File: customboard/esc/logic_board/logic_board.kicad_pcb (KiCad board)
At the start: 4 copper layers, 18.3 x 28.1 mm, 112 parts, among them J1 Conn_01x11, J2 Conn_01x03, J3 Conn_01x06, J4 Conn_01x11, J5 Conn_01x02, J6 Conn_01x02, J7 Conn_01x06, J8 Conn_01x03, U1 STM32F051K8Ux, U2 DRV8300DRGE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

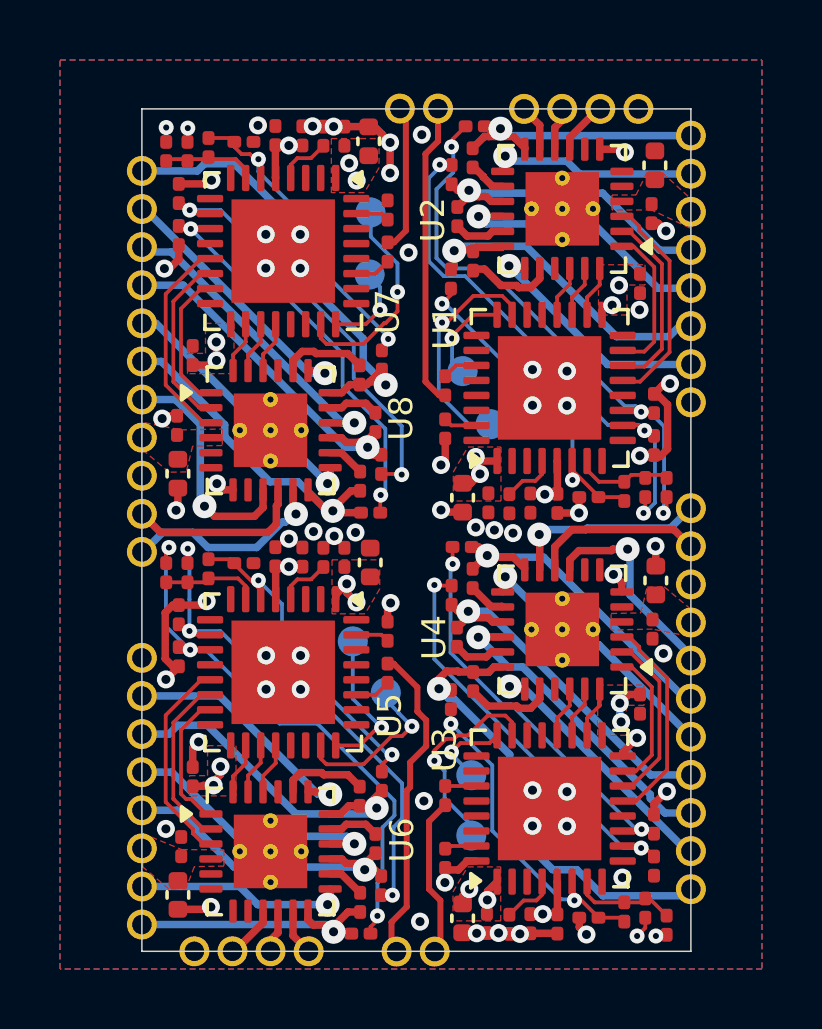
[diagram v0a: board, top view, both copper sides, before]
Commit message: power board done, minor fixes in logic board
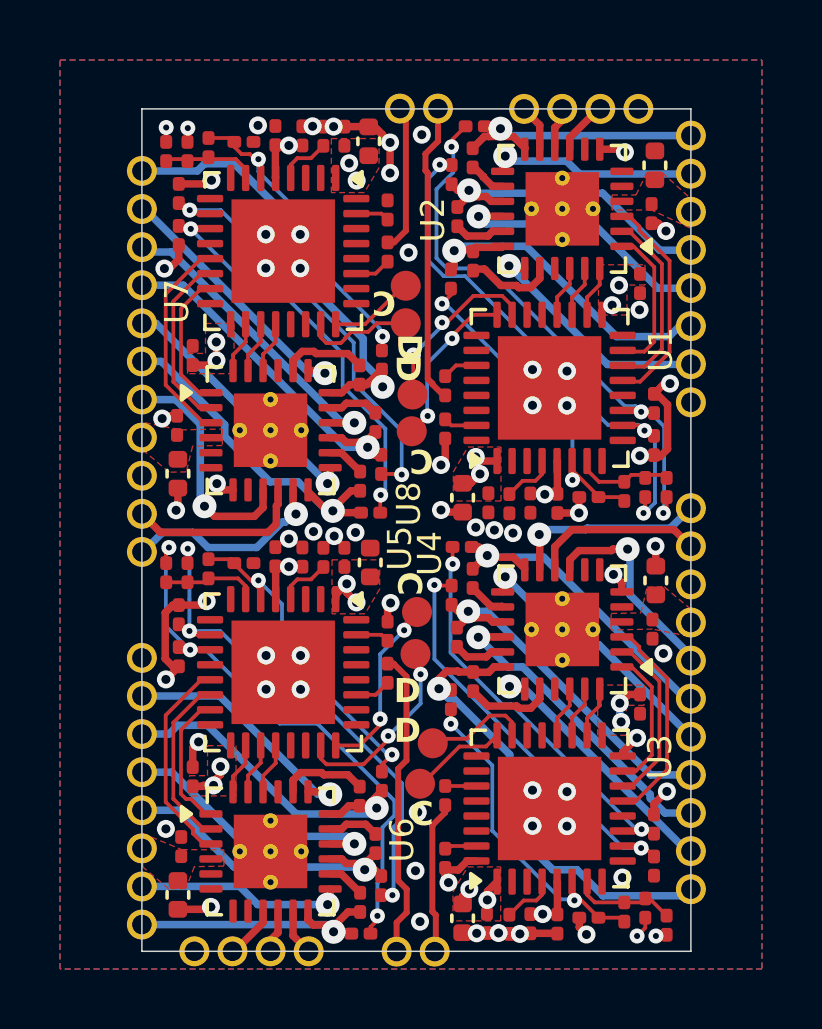
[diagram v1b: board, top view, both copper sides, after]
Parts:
- TP1, TP2, TP3, TP4, TP5, TP6, TP7, TP8: footprint TestPoint:TestPoint_Pad_D1.0mm -> Custom:SW_Testpoint; moved to F.Cu
- moved TP8 3.88 mm to (160.9, 151.6)
- moved TP4 3.33 mm to (161.8, 165.6)
- moved TP1 2.78 mm to (161.1, 154.0)
- moved TP3 2.63 mm to (161.1, 155.2)
- moved TP5 2.35 mm to (161.2, 161.2)
- moved TP2 1.73 mm to (161.3, 167.0)
- moved TP6 1.63 mm to (161.2, 162.7)
- moved TP7 1.26 mm to (160.9, 150.4)
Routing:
- net /Esc4/SWDIO: track 7.10 -> 3.64 mm, vias 1 -> 0
- net /Esc2/SWDIO: track 6.91 -> 3.60 mm, vias 1 -> 0
- net /Esc1/SWCLK: track 3.10 -> 5.56 mm, vias 1 -> 2
- net /Esc1/SWDIO: track 7.69 -> 5.94 mm, vias 1 -> 2
- net /Esc3/SWDIO: track 5.55 -> 6.48 mm, vias 1 -> 2
- net /Esc3/SWCLK: track 5.13 -> 6.04 mm, vias 1 -> 2
- net /Esc2/SWCLK: track 2.77 -> 3.24 mm, vias 1 -> 0
- net /Esc4/SWCLK: track 2.94 -> 2.72 mm, vias 1 -> 0
- net GND: vias 62 -> 63
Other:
- board text added: "C"
- board text added: "D"
- board text removed: "SWCLK"
- board text removed: "SWDIO"

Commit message: logic board 3v3 split
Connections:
- C1 pad 2: +3.3V -> /3V3_Right
- C12 pad 2: +3.3V -> /3V3_Left
- C13 pad 2: +3.3V -> /3V3_Left
- C14 pad 2: +3.3V -> /3V3_Right
- C15 pad 2: +3.3V -> /3V3_Right
- C16 pad 2: +3.3V -> /3V3_Right
- C18 pad 1: +3.3V -> /3V3_Right
- C19 pad 2: +3.3V -> /3V3_Right
- C2 pad 2: +3.3V -> /3V3_Right
- C26 pad 2: +3.3V -> /3V3_Left
- C27 pad 1: +3.3V -> /3V3_Left
- C28 pad 2: +3.3V -> /3V3_Left
- C34 pad 2: +3.3V -> /3V3_Left
- C35 pad 2: +3.3V -> /3V3_Left
- C37 pad 2: +3.3V -> /3V3_Left
- C38 pad 1: +3.3V -> /3V3_Left
- C39 pad 2: +3.3V -> /3V3_Left
- C4 pad 2: +3.3V -> /3V3_Right
- C5 pad 1: +3.3V -> /3V3_Right
- C6 pad 2: +3.3V -> /3V3_Right
- J3 pad 8: +3.3V -> /3V3_Left
- J7 pad 8: +3.3V -> /3V3_Right
- U1 pad 1: +3.3V -> /3V3_Right
- U1 pad 17: +3.3V -> /3V3_Right
- U1 pad 5: +3.3V -> /3V3_Right
- U3 pad 1: +3.3V -> /3V3_Right
- U3 pad 17: +3.3V -> /3V3_Right
- U3 pad 5: +3.3V -> /3V3_Right
- U5 pad 1: +3.3V -> /3V3_Left
- U5 pad 17: +3.3V -> /3V3_Left
- U5 pad 5: +3.3V -> /3V3_Left
- U7 pad 1: +3.3V -> /3V3_Left
- U7 pad 17: +3.3V -> /3V3_Left
- U7 pad 5: +3.3V -> /3V3_Left
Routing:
- net +3.3V: track 16.9 -> 0.00 mm, vias 20 -> 0
- net /3V3_Left: track 0.00 -> 8.48 mm, vias 0 -> 10
- net /3V3_Right: track 0.00 -> 8.40 mm, vias 0 -> 10
- added copper zone on F.Cu, net /3V3_Left
- added copper zone on In2.Cu, net /3V3_Left
- added copper zone on F.Cu, net /3V3_Right
- added copper zone on In2.Cu, net /3V3_Right
- removed copper zone on F.Cu, net +3.3V
- removed copper zone on In2.Cu, net +3.3V

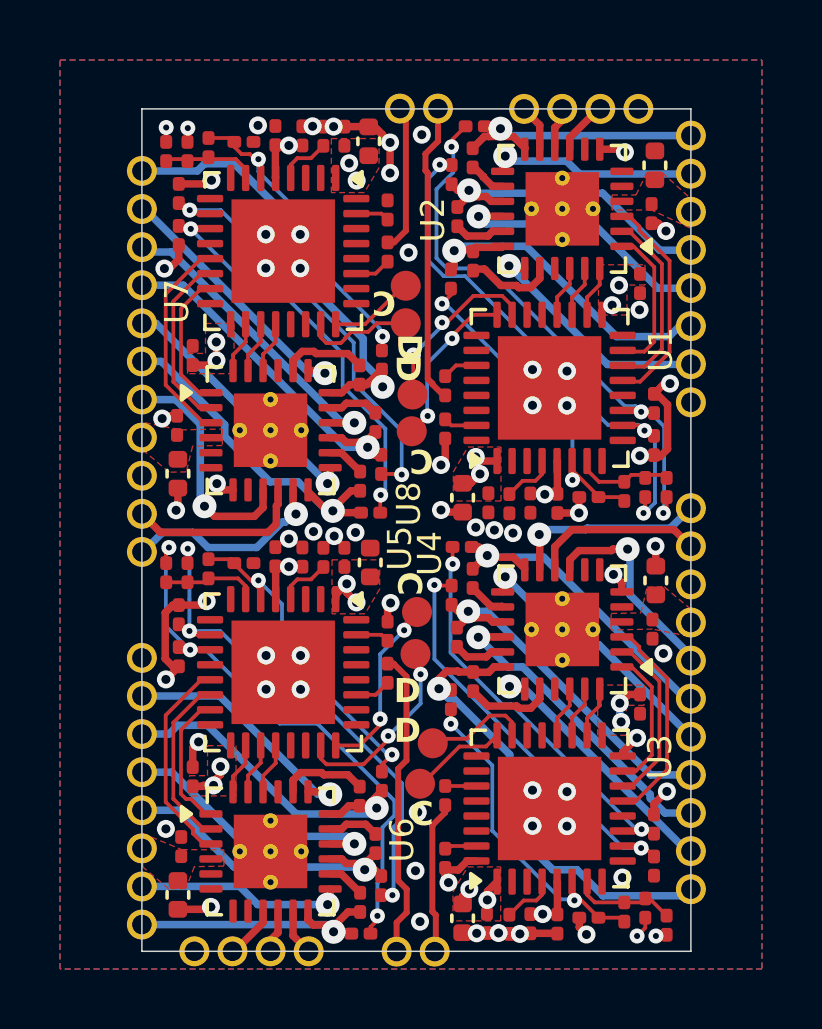
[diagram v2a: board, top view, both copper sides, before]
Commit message: narrower castelations on logic board; proper stls
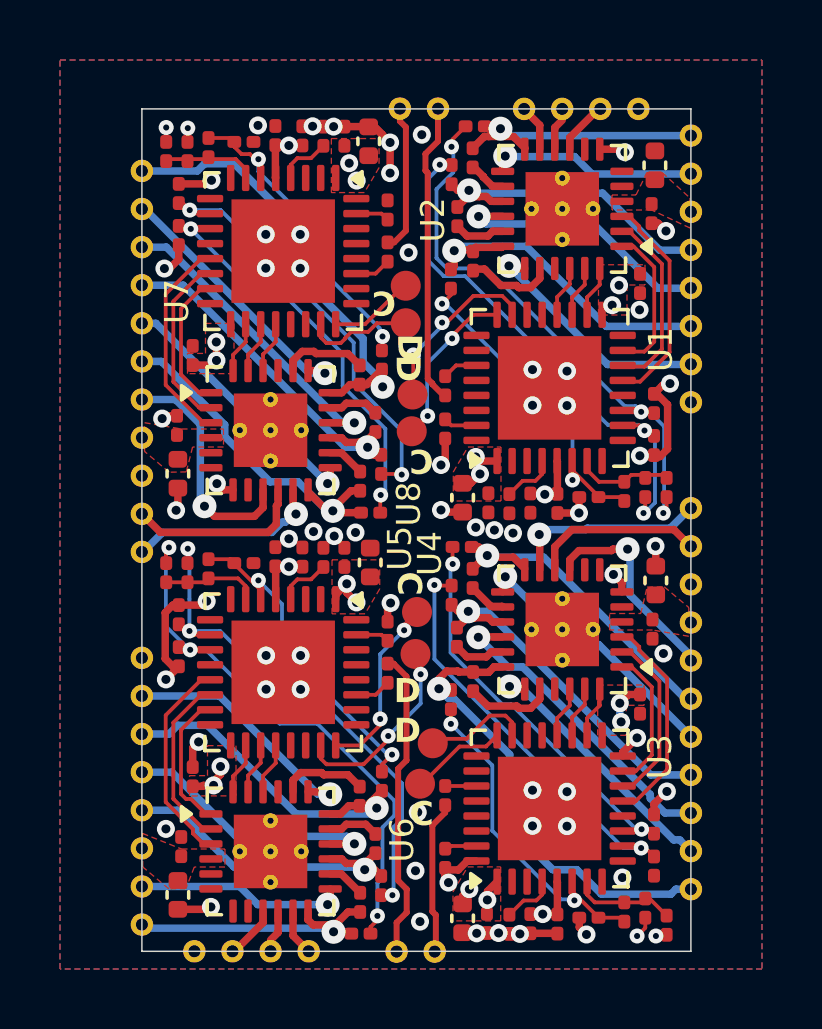
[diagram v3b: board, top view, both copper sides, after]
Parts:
- C1, C12, C13, C14, C15, C17, C2, C21, C25, C3, C30, C34, C35, C36, C41, C8: value 100n -> 100n 10V
- C10, C11, C18, C22, C23, C24, C27, C31, C32, C33, C38, C42, C43, C44, C5, C9: value 1u -> 1u 10V
- C16, C20, C26, C29, C37, C4, C40, C7: value 10u -> 10u 10V
- C19, C28, C39, C6: value 10n -> 10n 16V
